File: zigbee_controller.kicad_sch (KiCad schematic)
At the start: 59 parts, among them J1 +24V, J10 IO23 load, J11 IO20 load, J12 IO22 load, J13 IO21 load, J2 5v, J3 Conn_01x06, J4 Conn_01x07, J5 Conn_01x05, P1 USB_C_Plug_USB2.0, Q2 IRLB3813, Q3 IRLB3813, Q4 IRLB3813, Q5 IRLB3813, SW2 EN, SW4 Boot, U1 TPS54560, U2 ESP32-C6-MINI-1, U3 AMS1117-3.3, U4 TC4427, U5 TC4427

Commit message: Product in a working endstate
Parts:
- removed R1: 1.5kΩ, Resistor_SMD:R_1206_3216Metric_Pad1.30x1.75mm_HandSolder, symbol Device:R
- R6: value 10kΩ -> 13k
- R8: value 51kΩ -> 68k
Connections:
- net at R8.2: now also R6.1, U1.5 (FB)
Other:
- moved on the sheet: R8
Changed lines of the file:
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@@
 	)
 	(junction
-		(at 185.42 27.94)
+		(at 134.62 27.94)
 		(diameter 0)
 		(color 0 0 0 0)
 	)
 	(junction
-		(at 134.62 27.94)
+		(at 207.01 127)
 		(diameter 0)
 		(color 0 0 0 0)
 	)
 	(junction
-		(at 207.01 127)
+		(at 78.74 46.99)
 		(diameter 0)
 		(color 0 0 0 0)
 	)
 	(junction
-		(at 78.74 46.99)
+		(at 185.42 54.61)
 		(diameter 0)
 		(color 0 0 0 0)
@@
 	)
 	(junction
-		(at 185.42 54.61)
-		(diameter 0)
-		(color 0 0 0 0)
-	)
-	(junction
 		(at 121.92 81.28)
 		(diameter 0)
@@
 	)
 	(junction
+		(at 185.42 27.94)
+		(diameter 0)
+		(color 0 0 0 0)
+	)
+	(junction
 		(at 62.23 46.99)
 		(diameter 0)
@@
 	(wire
 		(pts
-			(xy 185.42 46.99) (xy 185.42 54.61)
-		)
-		(stroke
-			(width 0)
-			(type default)
-		)
-	)
-	(wire
-		(pts
 			(xy 261.62 120.65) (xy 265.43 120.65)
 		)
@@
 	(wire
 		(pts
-			(xy 185.42 35.56) (xy 185.42 39.37)
-		)
-		(stroke
-			(width 0)
-			(type default)
-		)
-	)
-	(wire
-		(pts
 			(xy 109.22 148.59) (xy 109.22 149.86)
 		)
@@
 	(wire
 		(pts
+			(xy 185.42 43.18) (xy 185.42 54.61)
+		)
+		(stroke
+			(width 0)
+			(type default)
+		)
+	)
+	(wire
+		(pts
 			(xy 207.01 115.57) (xy 219.71 115.57)
 		)
@@
 	(wire
 		(pts
+			(xy 185.42 35.56) (xy 185.42 27.94)
+		)
+		(stroke
+			(width 0)
+			(type default)
+		)
+	)
+	(wire
+		(pts
 			(xy 36.83 113.03) (xy 38.1 113.03)
 		)
@@
 	)
 	(symbol
-		(lib_id "Device:R")
-		(at 185.42 43.18 0)
-		(unit 1)
-		(body_style 1)
-		(exclude_from_sim no)
-		(in_bom yes)
-		(on_board yes)
-		(in_pos_files yes)
-		(dnp no)
-		(property "Reference" "R1"
-			(at 187.96 41.9099 0)
-			(show_name no)
-			(do_not_autoplace no)
-			(effects
-				(font
-					(size 1.27 1.27)
-				)
-				(justify left)
-			)
-		)
-		(property "Value" "1.5kΩ"
-			(at 187.96 44.45 0)
-			(show_name no)
-			(do_not_autoplace no)
-			(effects
-				(font
-					(size 1.27 1.27)
-				)
-				(justify left)
-			)
-		)
-		(property "Footprint" "Resistor_SMD:R_1206_3216Metric_Pad1.30x1.75mm_HandSolder"
-			(at 183.642 43.18 90)
-			(hide yes)
-			(show_name no)
-			(do_not_autoplace no)
-			(effects
-				(font
-					(size 1.27 1.27)
-				)
-			)
-		)
-		(property "Datasheet" ""
-			(at 185.42 43.18 0)
-			(hide yes)
-			(show_name no)
-			(do_not_autoplace no)
-			(effects
-				(font
-					(size 1.27 1.27)
-				)
-			)
-		)
-		(property "Description" "Resistor"
-			(at 185.42 43.18 0)
-			(hide yes)
-			(show_name no)
-			(do_not_autoplace no)
-			(effects
-				(font
-					(size 1.27 1.27)
-				)
-			)
-		)
-		(pin "1"
-		)
-		(pin "2"
-		)
-		(instances
-			(project "zigbee_controller"
-				(path "/17b9f9ac-224d-422f-9c40-54a6770d01d0"
-					(reference "R1")
-					(unit 1)
-				)
-			)
-		)
-	)
-	(symbol
 		(lib_id "power:+3V3")
 		(at 260.35 73.66 0)
@@
 			)
 		)
-		(property "Value" "10kΩ"
+		(property "Value" "13k"
 			(at 187.96 62.2299 0)
 			(show_name no)
@@
 	(symbol
 		(lib_id "Device:R")
-		(at 185.42 31.75 0)
+		(at 185.42 39.37 0)
 		(unit 1)
 		(body_style 1)
@@
 		(dnp no)
 		(property "Reference" "R8"
-			(at 187.96 30.4799 0)
+			(at 187.96 38.0999 0)
 			(show_name no)
 			(do_not_autoplace no)
@@
 			)
 		)
-		(property "Value" "51kΩ"
-			(at 187.96 33.02 0)
+		(property "Value" "68k"
+			(at 187.96 40.64 0)
 			(show_name no)
 			(do_not_autoplace no)
@@
 		)
 		(property "Footprint" "Resistor_SMD:R_1206_3216Metric_Pad1.30x1.75mm_HandSolder"
-			(at 183.642 31.75 90)
+			(at 183.642 39.37 90)
 			(hide yes)
 			(show_name no)
@@
 		)
 		(property "Datasheet" ""
-			(at 185.42 31.75 0)
+			(at 185.42 39.37 0)
 			(hide yes)
 			(show_name no)
@@
 		)
 		(property "Description" "Resistor"
-			(at 185.42 31.75 0)
+			(at 185.42 39.37 0)
 			(hide yes)
 			(show_name no)
@@
 			"27f51bee-280e-44b6-83a5-66eecb7ea94d" "2823f51f-40f7-4632-b994-192965936578"
 			"291e06bc-6f99-462f-96d7-f263d04362d4" "2abbef87-a15d-4269-bec1-96cc22601fa2"
-			"2ca4a27b-fc05-4f6f-b433-4f44aaceaad6" "2efc59b9-1eba-4bfa-93e8-a9f3bc7e101b"
 			"2f64733e-1b2c-4725-8d42-8fddda4cb43a" "30d67de4-5f7f-4852-9a22-c44a3bebfb40"
 			"32040ff5-857e-4036-b6c7-2eae787d98ea" "32107fd9-14e2-465c-aa5b-2ab5b1a8d604"
@@
 			"376d6545-fae6-4fb3-9d48-2843365d77ce" "393ae429-135c-4e3e-86e3-cc2cf12f49e8"
 			"39794c0d-c614-4c12-b4e9-afef67cc0e59" "3ae3b833-e0d2-4c9b-bcb4-ae9969d73db3"
-			"3c429a5c-1f8c-4958-9085-dbb5334cb8ab" "3c4702f1-285b-406a-b579-7fba264822f4"
-			"3d17fc58-9116-49af-9d58-e6ea6531c3d2" "41275b0b-6267-4ed6-8cfb-103103581dd3"
-			"41a5d517-2b18-461b-bb38-84204afeabc0" "4323ddec-fcbb-414d-bc60-a374826c0b22"
-			"4662acbd-9b89-43f4-8920-1cf1da32fd91" "49cdf3b3-9528-4901-85b3-bc5cffb0152a"
-			"4a74262b-913d-402d-8e57-6bc807178dd3" "4b51df57-7cf3-4fca-81e2-88b63b68140a"
-			"4d4e16e6-3d43-40db-8694-ba7849f79cab" "4f783318-3851-4e39-96aa-2c9d7597610e"
-			"5131cf46-d23c-41aa-ba69-aa15ca4b748e" "5254b13a-e5df-4355-bda6-abb30a3d7386"
-			"5275d6ac-584b-40f1-8e15-d93707cd91be" "559457ec-f4f7-432a-9ad2-99716797ae57"
-			"55d64d9f-b920-44fd-8d1a-d33763254af1" "58266d41-8262-4d2c-8e89-47a594561037"
-			"5d3360b5-6f13-4074-839e-b842a88d699b" "614c3105-482c-4773-9716-a01b476ea010"
-			"616f3177-b9b0-44bb-a30f-a246a3a9ad18" "62a621e2-196e-49fe-a2dc-04003a3a8868"
-			"63a7544d-84c9-45ae-8919-cf2de06927be" "64617598-29b5-4b94-af8c-06334d7082bb"
-			"65c20d66-ae4b-4be5-a06d-18f5466c4228" "672ad2db-60b6-4027-960c-2bd563c678c8"
-			"69e4687b-504c-448f-8b0f-3a22a5c0e48a" "6a999cfb-c089-4328-acae-ce8da364548b"
-			"6d42bae0-c332-4f3c-85e6-5751c803f4fa" "6fee591d-130d-4980-a2eb-388d59e64c52"
-			"73caed4c-d89e-408b-bcb4-e6d59a4f2267" "78b40dd6-f29b-46b9-bc3c-bf3bfee4b470"
-			"78cb1773-4776-4949-973d-0c10ff975984" "7bdd1370-37e1-4a46-86bd-23ac2c860b37"
+			"3bbaf09f-9e15-422b-9d55-ad5784eb6105" "3c429a5c-1f8c-4958-9085-dbb5334cb8ab"
+			"3c4702f1-285b-406a-b579-7fba264822f4" "3d17fc58-9116-49af-9d58-e6ea6531c3d2"
+			"41275b0b-6267-4ed6-8cfb-103103581dd3" "41a5d517-2b18-461b-bb38-84204afeabc0"
+			"4323ddec-fcbb-414d-bc60-a374826c0b22" "4662acbd-9b89-43f4-8920-1cf1da32fd91"
+			"49cdf3b3-9528-4901-85b3-bc5cffb0152a" "4a74262b-913d-402d-8e57-6bc807178dd3"
+			"4b51df57-7cf3-4fca-81e2-88b63b68140a" "4d4e16e6-3d43-40db-8694-ba7849f79cab"
+			"4f783318-3851-4e39-96aa-2c9d7597610e" "5131cf46-d23c-41aa-ba69-aa15ca4b748e"
+			"5254b13a-e5df-4355-bda6-abb30a3d7386" "5275d6ac-584b-40f1-8e15-d93707cd91be"
+			"559457ec-f4f7-432a-9ad2-99716797ae57" "55d64d9f-b920-44fd-8d1a-d33763254af1"
+			"58266d41-8262-4d2c-8e89-47a594561037" "5d3360b5-6f13-4074-839e-b842a88d699b"
+			"614c3105-482c-4773-9716-a01b476ea010" "616f3177-b9b0-44bb-a30f-a246a3a9ad18"
+			"62a621e2-196e-49fe-a2dc-04003a3a8868" "63a7544d-84c9-45ae-8919-cf2de06927be"
+			"64617598-29b5-4b94-af8c-06334d7082bb" "65c20d66-ae4b-4be5-a06d-18f5466c4228"
+			"672ad2db-60b6-4027-960c-2bd563c678c8" "69e4687b-504c-448f-8b0f-3a22a5c0e48a"
+			"6a999cfb-c089-4328-acae-ce8da364548b" "6d42bae0-c332-4f3c-85e6-5751c803f4fa"
+			"6fee591d-130d-4980-a2eb-388d59e64c52" "73caed4c-d89e-408b-bcb4-e6d59a4f2267"
+			"78b40dd6-f29b-46b9-bc3c-bf3bfee4b470" "78cb1773-4776-4949-973d-0c10ff975984"
 			"7d810b1a-1f62-4858-98a4-0cf53ac5a21e" "7f6c6605-41f0-4ed3-b6bf-d532a1e7d5ec"
-			"80bb56dc-e87d-42a0-97f9-51709edcb93a" "832b2a72-2ce8-4584-8e79-46a21adfa1a7"
-			"8335660f-3f10-4fdd-9c2d-350108056eeb" "851058d4-472c-402e-b18c-b4e9a9134c31"
+			"80bb56dc-e87d-42a0-97f9-51709edcb93a" "851058d4-472c-402e-b18c-b4e9a9134c31"
 			"877f21ae-f420-468a-a917-b5fb6fefbf57" "878a5696-02cc-46fa-a732-96650e32d470"
 			"8857cb86-e42c-4bfe-b49f-2e0a58b23994" "8aac1dba-682a-4c74-a23c-c8dfbd82be4f"
@@
 			"bf81eefc-dfb1-4ef1-bccc-2cde9ef36a32" "c2724638-839b-4cae-bd71-4692d46ee7c1"
 			"c4ab9468-c2f6-4b7a-ac75-5326684fb3b3" "c55869b3-7c8a-4ab8-a8c9-64925e73cb42"
-			"ca6aeab7-ec32-4766-8331-a0343c305c20" "cac4e678-ed8c-402b-8ca2-c42500ed8cb4"
-			"ceae6497-9193-4c85-b4ed-42ba2ccbd40c" "cf584716-7a72-45b8-b2b3-1ffe671e30de"
-			"d04046bc-0d14-4ab5-813d-df2f1ff28395" "d04d8dc5-e5e1-4cd2-9658-1c4abe024e89"
-			"d64f5836-4103-4a84-9dd5-1f7f0305f60e" "d73927b4-793d-4595-8aaf-50ea464e0738"
-			"d8c581fe-79b2-4249-9c5c-a3b900102f7f" "d8d73fd7-f6db-4287-bae5-9bba9eaf6b1e"
-			"d9a00c86-0de7-4ddd-a68a-25066c5bd9ec" "da15ab7c-eb15-4e17-a4e3-56534557d883"
-			"dc08dfb9-c5bd-45c4-a8fb-53c28003770e" "ddd026ea-917b-4a52-a031-e6b4d5327bea"
-			"dfa89d7a-d5d1-4cd8-b896-e67718d3610c" "e1a6d7ab-0efd-4aa1-adf1-03057288866c"
+			"c6c1cc1e-0b8f-4ed0-8072-a8f19c373285" "ca6aeab7-ec32-4766-8331-a0343c305c20"
+			"cac4e678-ed8c-402b-8ca2-c42500ed8cb4" "ceae6497-9193-4c85-b4ed-42ba2ccbd40c"
+			"cf584716-7a72-45b8-b2b3-1ffe671e30de" "d04046bc-0d14-4ab5-813d-df2f1ff28395"
+			"d04d8dc5-e5e1-4cd2-9658-1c4abe024e89" "d64f5836-4103-4a84-9dd5-1f7f0305f60e"
+			"d73927b4-793d-4595-8aaf-50ea464e0738" "d8c581fe-79b2-4249-9c5c-a3b900102f7f"
+			"d8d73fd7-f6db-4287-bae5-9bba9eaf6b1e" "d9a00c86-0de7-4ddd-a68a-25066c5bd9ec"
+			"da15ab7c-eb15-4e17-a4e3-56534557d883" "dc08dfb9-c5bd-45c4-a8fb-53c28003770e"
+			"ddd026ea-917b-4a52-a031-e6b4d5327bea" "dfa89d7a-d5d1-4cd8-b896-e67718d3610c"
+			"e18dbe84-9196-414d-8ce1-e2e35c00168b" "e1a6d7ab-0efd-4aa1-adf1-03057288866c"
 			"e35ee571-f46b-4b87-a1c3-0a3f2f9596a3" "e4628858-0e6e-4a69-a8b4-1ce264ece58b"
 			"e5b303f7-efc8-4679-88e5-78bffac98948" "e5f0b49a-5184-4c1d-9574-c16d0ea13899"
@@
 			"f3ca1fd3-6364-42b7-85d3-6b33ca17db2a" "f4004a81-67ee-496f-ba27-92ca1338b2fd"
 			"f8132236-eec2-4fb9-a06f-8c487b4fe1a0" "f907f5a7-56c1-42ae-bab1-210250c96c0f"
-			"faaca74b-823b-435c-92ce-e99667f9dcc3" "fc68a5ef-6011-4464-b696-76ab1fa512fa"
-			"fec0336b-d5bd-4d19-87ca-dfd0e88e1ba4" "ffb95fe5-0330-4aba-9656-be73aafe31a0"
+			"faaca74b-823b-435c-92ce-e99667f9dcc3" "faf2b8bb-cd39-4a98-8acb-2b915b8b691f"
+			"fc68a5ef-6011-4464-b696-76ab1fa512fa" "fec0336b-d5bd-4d19-87ca-dfd0e88e1ba4"
+			"ffb95fe5-0330-4aba-9656-be73aafe31a0"
 		)
 	)

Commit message: before making space for IO numbers
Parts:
- C5: value 0.1μF -> 100nF
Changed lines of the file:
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@@
 			)
 		)
-		(property "Value" "0.1μF"
+		(property "Value" "100nF"
 			(at 107.95 21.59 90)
 			(show_name no)

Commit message: before adding SS36
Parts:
- added R1, R5: 5k1, symbol Device:R
- added TP4: GND, TestPoint:TestPoint_THTPad_D2.0mm_Drill1.0mm, symbol Connector:TestPoint
- J5: now not fitted
- P1: value USB_C_Plug_USB2.0 -> USB_C_Receptacle_GCT_USB4105; symbol Connector:USB_C_Plug_USB2.0 -> Connector:USB_C_Receptacle_USB2.0_16P
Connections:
- net GND: now also R1.2, R5.2, TP4.1
- net IO12-usb: now also P1.B7 (D-)
- net IO13-usb: now also P1.B6 (D+)
- net at P1.A5 (CC1): now also R1.1
- net at P1.B5 (CC2): now also R5.1
- no-connect marks 9 -> 10

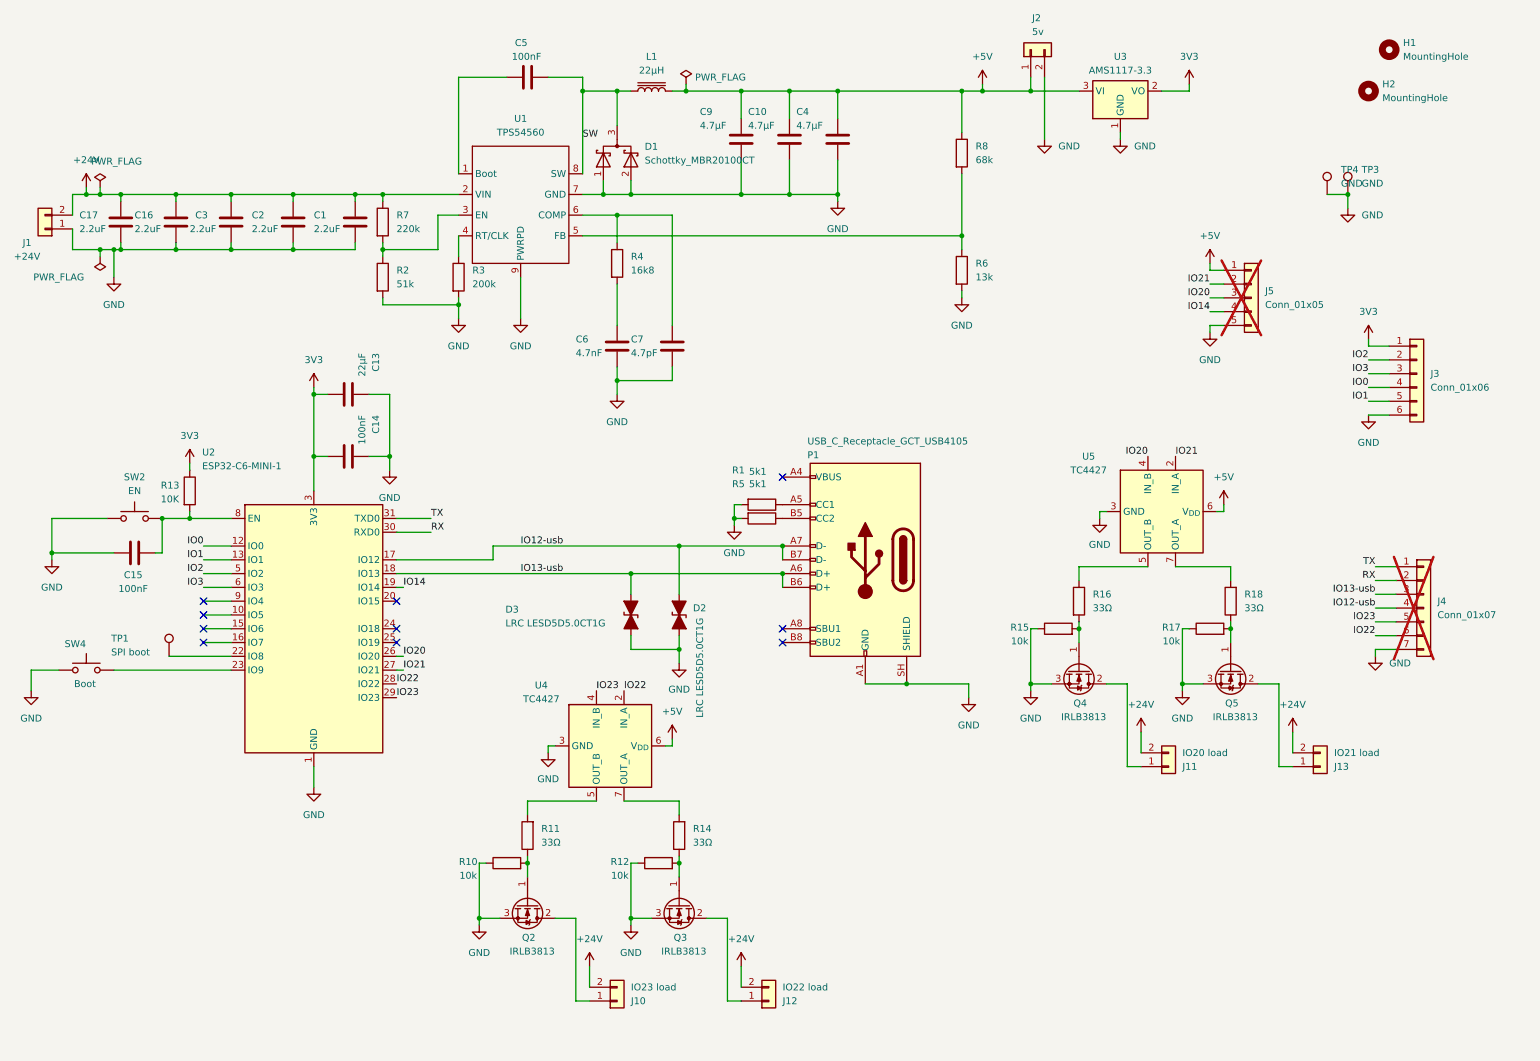
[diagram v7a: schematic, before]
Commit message: 4 Channels working, before adding 4 5v channel
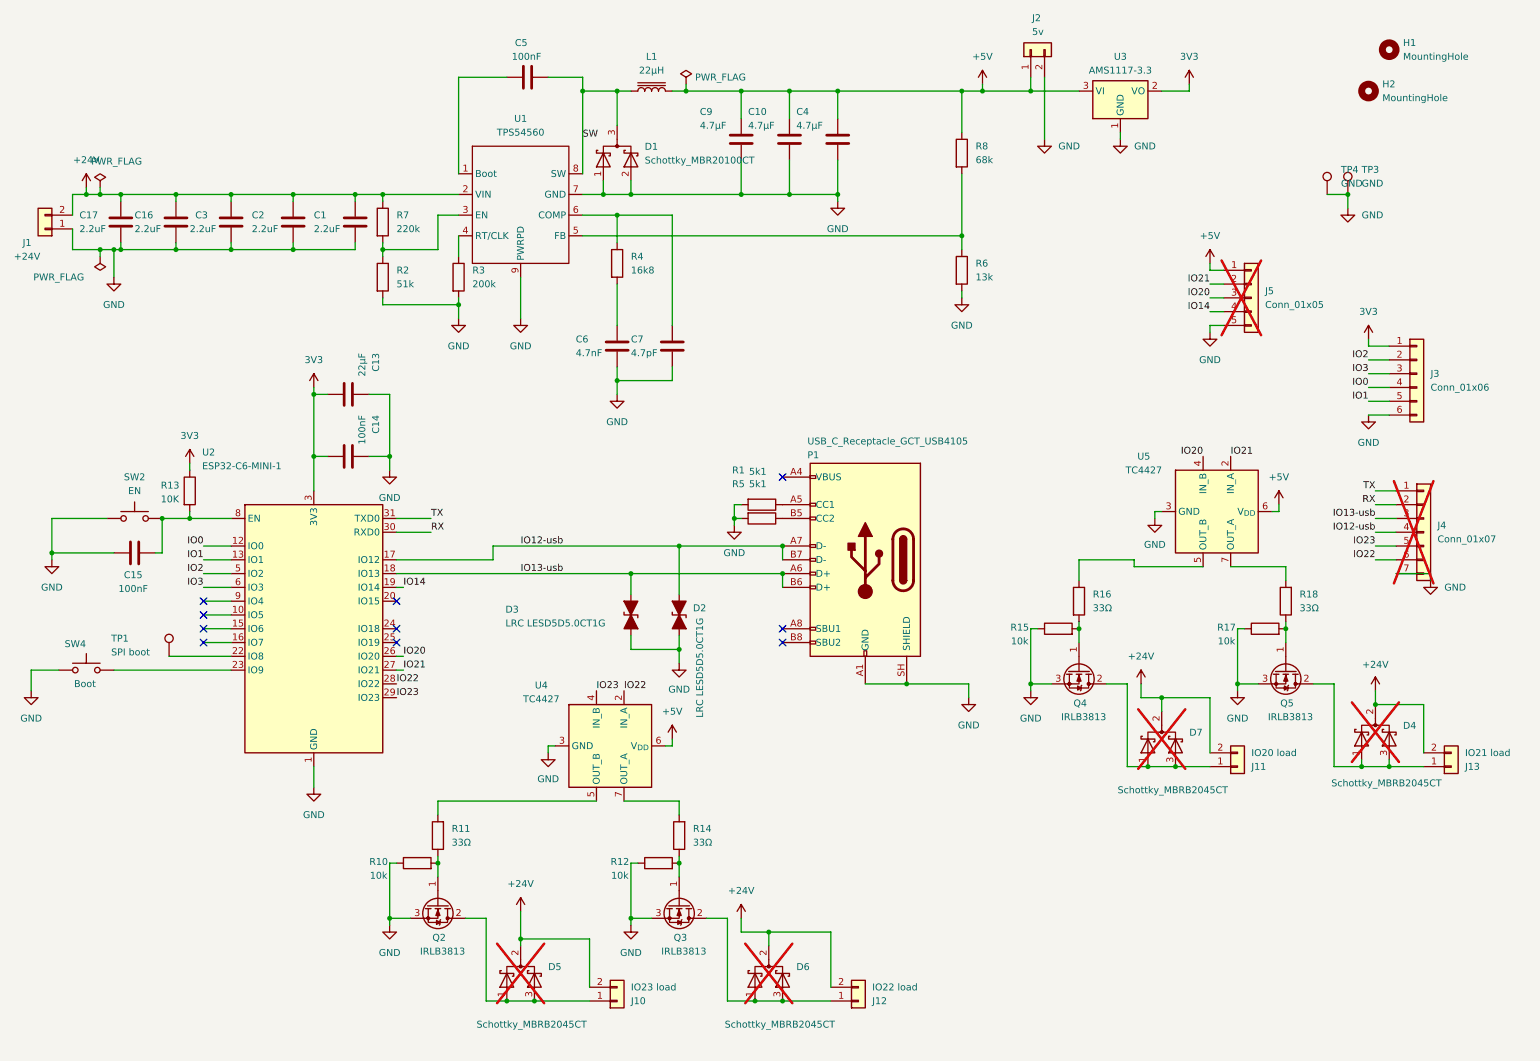
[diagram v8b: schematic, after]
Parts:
- added D4, D5, D6, D7: Schottky_MBRB2045CT, Package_TO_SOT_THT:TO-220-3_Vertical, symbol Device:D_Schottky_Dual_CommonCathode_AKA_Parallel
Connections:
- net +24V: now also D4.2 (K), D5.2 (K), D6.2 (K), D7.2 (K)
- net at J13.1 (Pin_1), Q5.2 (D): now also D4.1 (A), D4.3 (A)
- net at J12.1 (Pin_1), Q3.2 (D): now also D6.1 (A), D6.3 (A)
- net at J10.1 (Pin_1), Q2.2 (D): now also D5.1 (A), D5.3 (A)
- net at J11.1 (Pin_1), Q4.2 (D): now also D7.1 (A), D7.3 (A)
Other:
- moved on the sheet: J11, J12, J13, J4, Q2, Q5, R10, R11, R17, R18, U5
